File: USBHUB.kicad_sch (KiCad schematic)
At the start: 0 parts

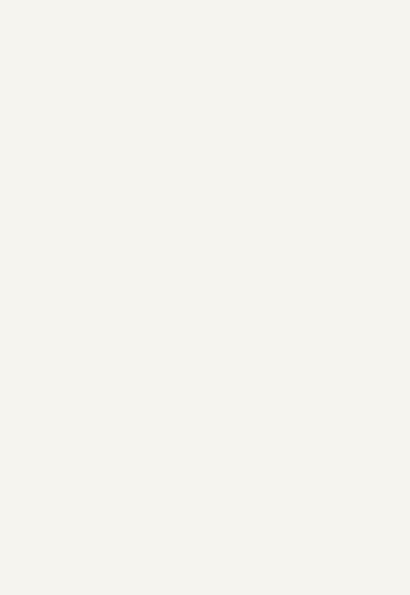
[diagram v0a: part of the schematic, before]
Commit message: finish PD controller schematic
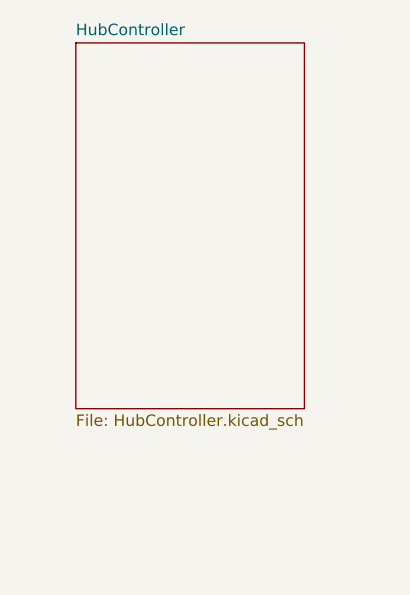
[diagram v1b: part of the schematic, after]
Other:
- added sheet HubController (HubController.kicad_sch)
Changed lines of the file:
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@@
     (title "USB Hub")
+  )
+  (sheet (at 31.75 50.8) (size 25.4 40.64) (fields_autoplaced)
+    (stroke (width 0.1524) (type solid))
+    (fill (color 0 0 0 0.0000))
+    (property "Sheetname" "HubController" (at 31.75 50.0884 0)
+      (effects (font (size 1.27 1.27)) (justify left bottom))
+    )
+    (property "Sheetfile" "HubController.kicad_sch" (at 31.75 92.0246 0)
+      (effects (font (size 1.27 1.27)) (justify left top))
+    )
+    (instances
+      (project "USBHUB"
+        (path "/d5edc647-9ac3-4ac1-ab8a-57c77be3f4d3" (page "3"))
+      )
+    )
   )
   (sheet (at 25.4 119.38) (size 21.59 35.56) (fields_autoplaced)

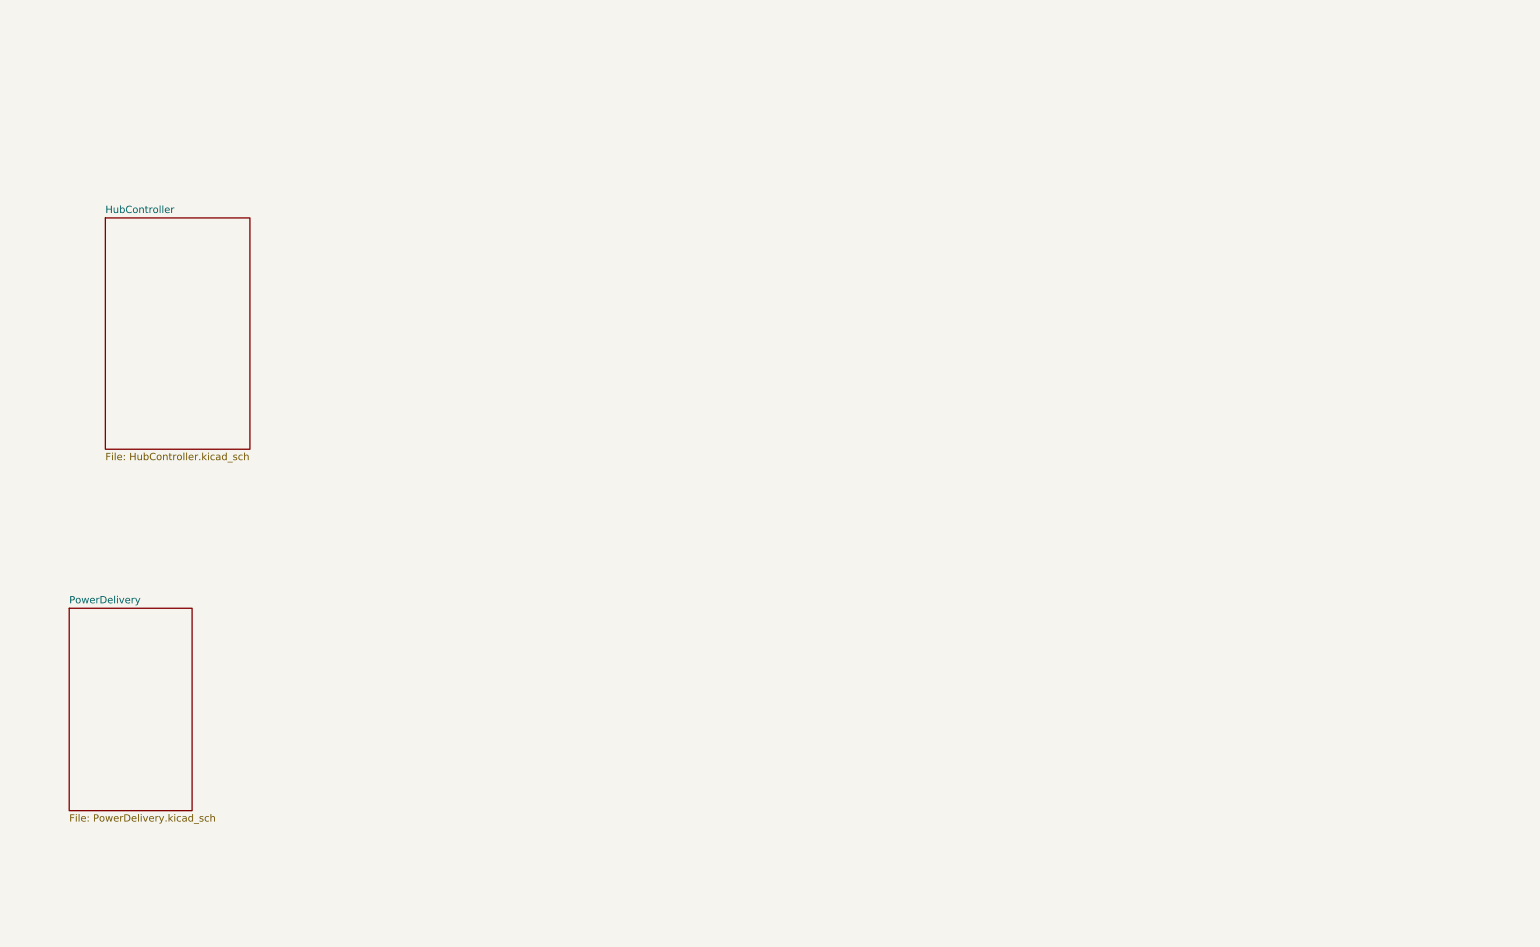
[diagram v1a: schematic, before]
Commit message: start layout of usb PD
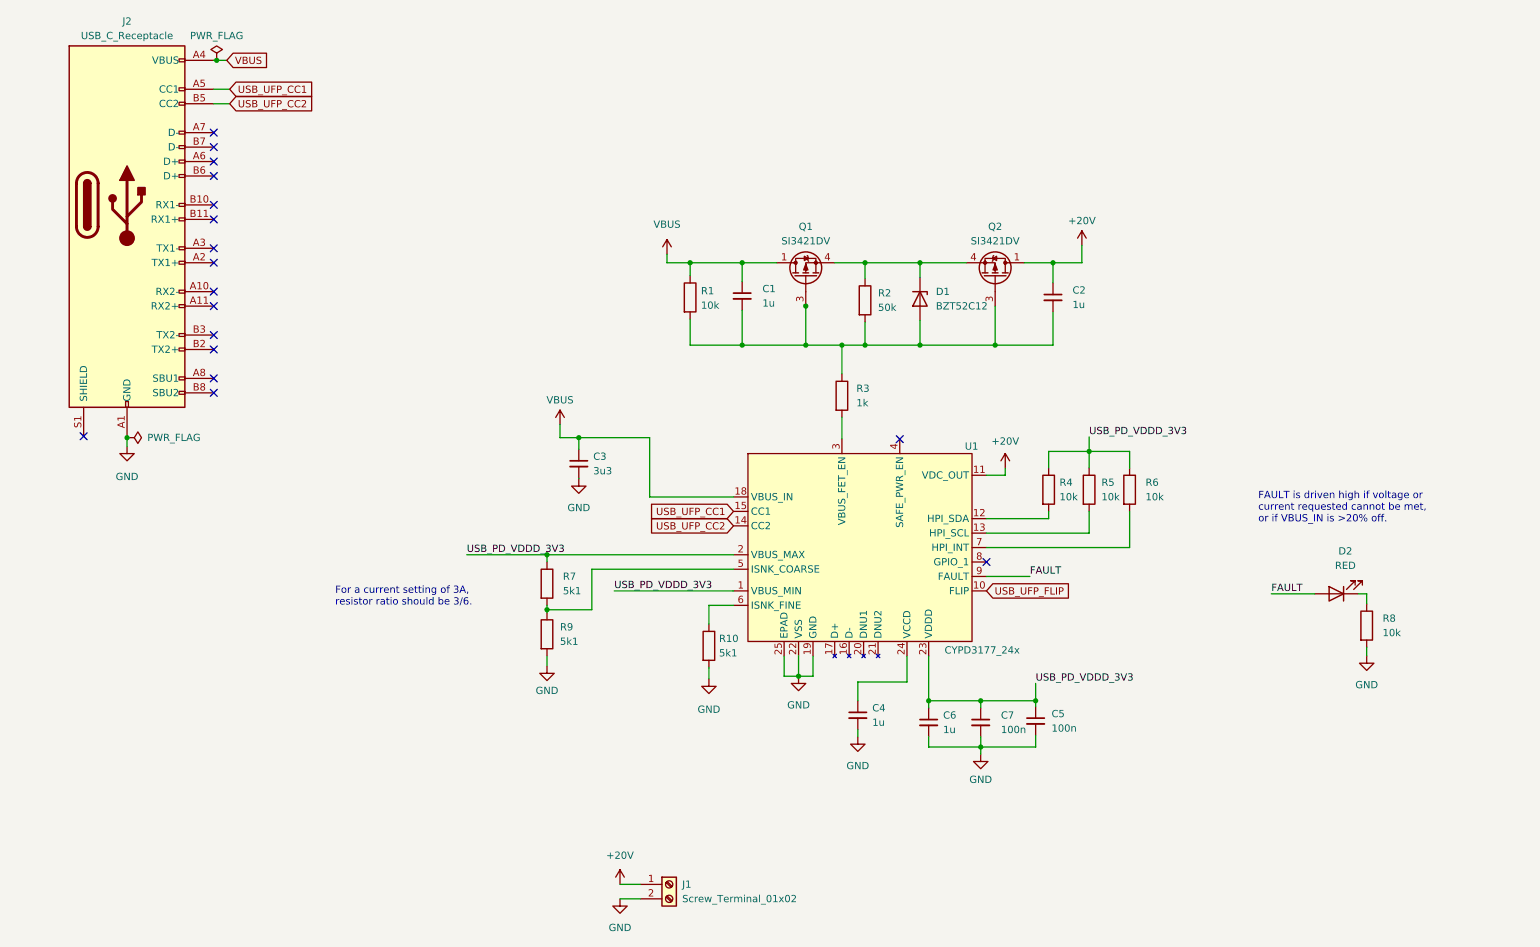
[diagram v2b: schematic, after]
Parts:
- added C1, C2, C4, C6: 1u, Capacitor_SMD:C_0603_1608Metric, symbol Device:C_Small
- added C3: 3u3, Capacitor_SMD:C_0603_1608Metric, symbol Device:C_Small
- added C5, C7: 100n, Capacitor_SMD:C_0603_1608Metric, symbol Device:C_Small
- added D1: BZT52C12, Diode_SMD:D_SOD-123, symbol Device:D_Zener
- added D2: RED, LED_SMD:LED_0603_1608Metric, symbol Device:LED
- added J1: Screw_Terminal_01x02, TerminalBlock_Phoenix:TerminalBlock_Phoenix_MKDS-1,5-2-5.08_1x02_P5.08mm_Horizontal, symbol Connector:Screw_Terminal_01x02
- added J2: USB_C_Receptacle, Cake_USB:USB_C_Receptacle_GT-USB-7052, symbol Connector:USB_C_Receptacle
- added Q1, Q2: SI3421DV, Package_TO_SOT_SMD:SOT-23-6, symbol catSink:SI3421DV
- added R1, R4, R5, R6, R8: 10k, Resistor_SMD:R_0603_1608Metric, symbol Device:R
- added R10, R7, R9: 5k1, Resistor_SMD:R_0603_1608Metric, symbol Device:R
- added R2: 50k, Resistor_SMD:R_0603_1608Metric, symbol Device:R
- added R3: 1k, Resistor_SMD:R_0603_1608Metric, symbol Device:R
- added U1: CYPD3177_24x, Cake_USB:CYPD3177_24LQx_QFN-24_EP_4x4_Pitch0.5mm, symbol Cake_USB:CYPD3177_24x
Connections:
- new net: D1.1 (K), Q1.4 (S), Q2.4 (S), R2.1
- new net: C1.2, C2.2, D1.2 (A), Q1.3 (G), Q2.3 (G), R1.2, R2.2, R3.1
- new net: R5.2, U1.13 (HPI_SCL)
- new net: R7.2, R9.1, U1.5 (ISNK_COARSE)
- new net: R4.2, U1.12 (HPI_SDA)
- new net: D2.1 (K), R8.1
- new net: C4.1, U1.24 (VCCD)
- new net: R3.2, U1.3 (VBUS_FET_EN)
- new net: R10.1, U1.6 (ISNK_FINE)
- new net: R6.2, U1.7 (HPI_INT)
- new net +20V: C2.1, J1.1 (Pin_1), Q2.1 (D), Q2.2 (D1), Q2.5 (D2), Q2.6 (D3), U1.11 (VDC_OUT)
- new net FAULT: D2.2 (A), U1.9 (FAULT)
- new net GND: C3.2, C4.2, C5.2, C6.2, C7.2, J1.2 (Pin_2), J2.A1 (GND), J2.A12 (GND), J2.B1 (GND), J2.B12 (GND), R10.2, R8.2, R9.2, U1.19 (GND), U1.22 (VSS), U1.25 (EPAD)
- new net USB_PD_VDDD_3V3: C5.1, C6.1, C7.1, R4.1, R5.1, R6.1, R7.1, U1.1 (VBUS_MIN), U1.2 (VBUS_MAX), U1.23 (VDDD)
- new net USB_UFP_CC1: J2.A5 (CC1), U1.15 (CC1)
- new net USB_UFP_CC2: J2.B5 (CC2), U1.14 (CC2)
- new net USB_UFP_FLIP: U1.10 (FLIP)
- new net VBUS: C1.1, C3.1, J2.A4 (VBUS), J2.A9 (VBUS), J2.B4 (VBUS), J2.B9 (VBUS), Q1.1 (D), Q1.2 (D1), Q1.5 (D2), Q1.6 (D3), R1.1, U1.18 (VBUS_IN)
- no-connect marks 0 -> 17
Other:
- removed sheet HubController
- removed sheet PowerDelivery
- note added: "FAULT is driven high if voltage or current requested cannot be met, or if VBUS_IN is >20% off."
- note added: "For a current setting of 3A, resistor ratio should be 3/6."
- title: USB Hub -> USB PD

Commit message: Finish PCB design
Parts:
- added C8: 3u3, Capacitor_SMD:C_0603_1608Metric, symbol Device:C_Small
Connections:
- net +20V: now also J1.2 (Pin_2), C8.1; no longer J1.1 (Pin_1)
- net GND: now also J1.1 (Pin_1), C8.2; no longer J1.2 (Pin_2)
- net USB_UFP_FLIP: no longer names the net of U1.10 (FLIP)
- no-connect marks 17 -> 18
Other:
- moved on the sheet: D2, J1, R8

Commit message: some touchups
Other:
- note added: "FAULT LED"
- note added: "USB P/D 20V/3A"
- moved on the sheet: C8, J1, J2

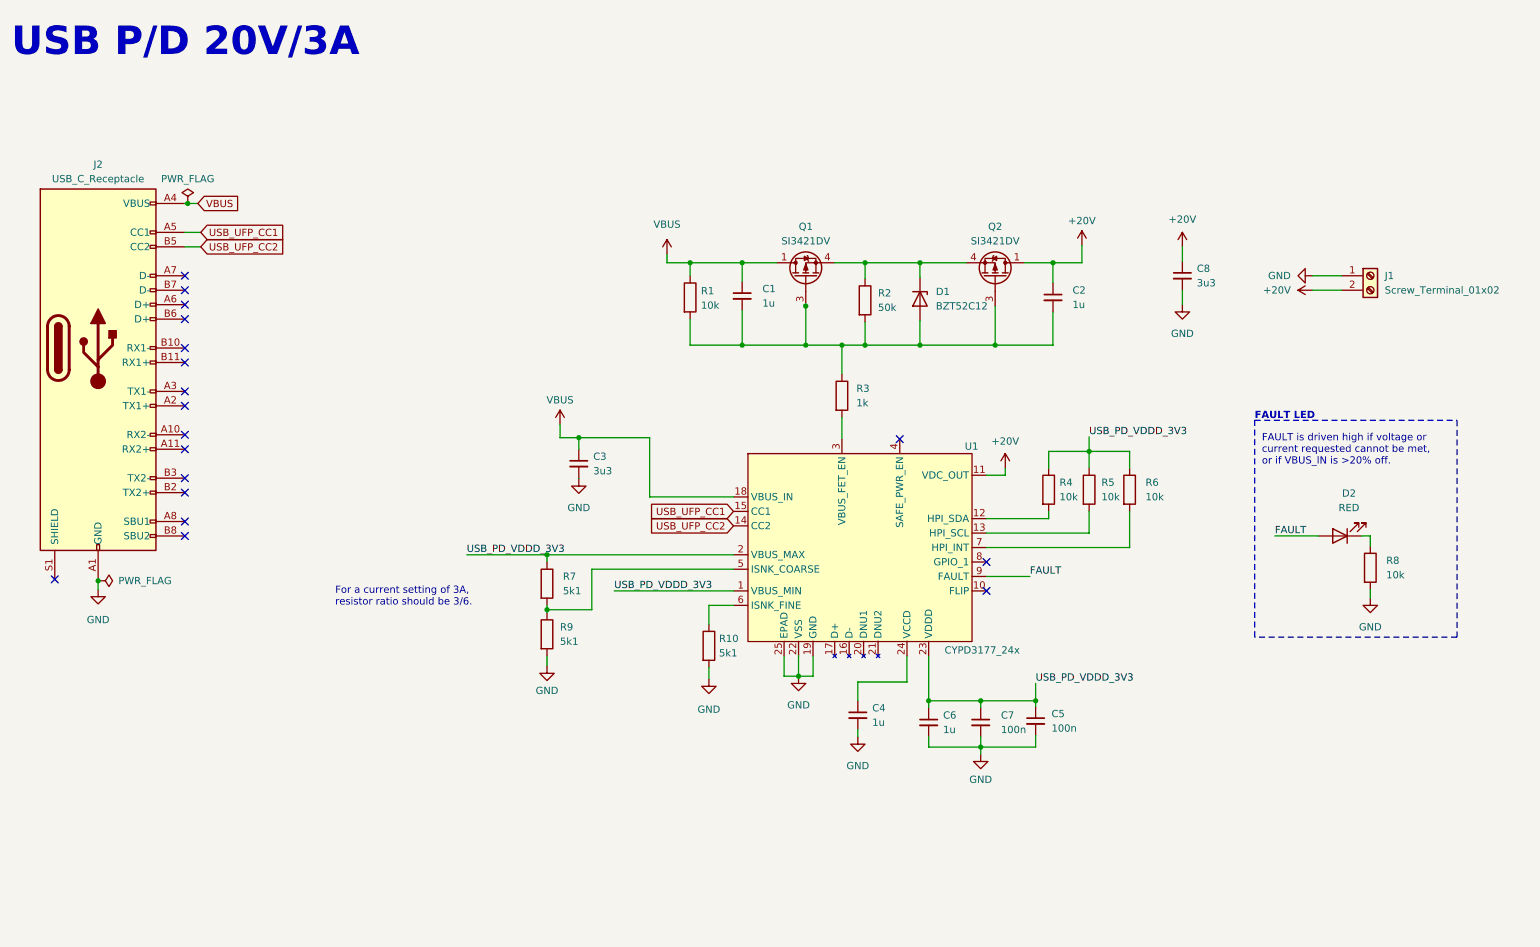
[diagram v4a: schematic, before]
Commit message: Add ESD for usb parts research, add TUSB522P and PI3USB302
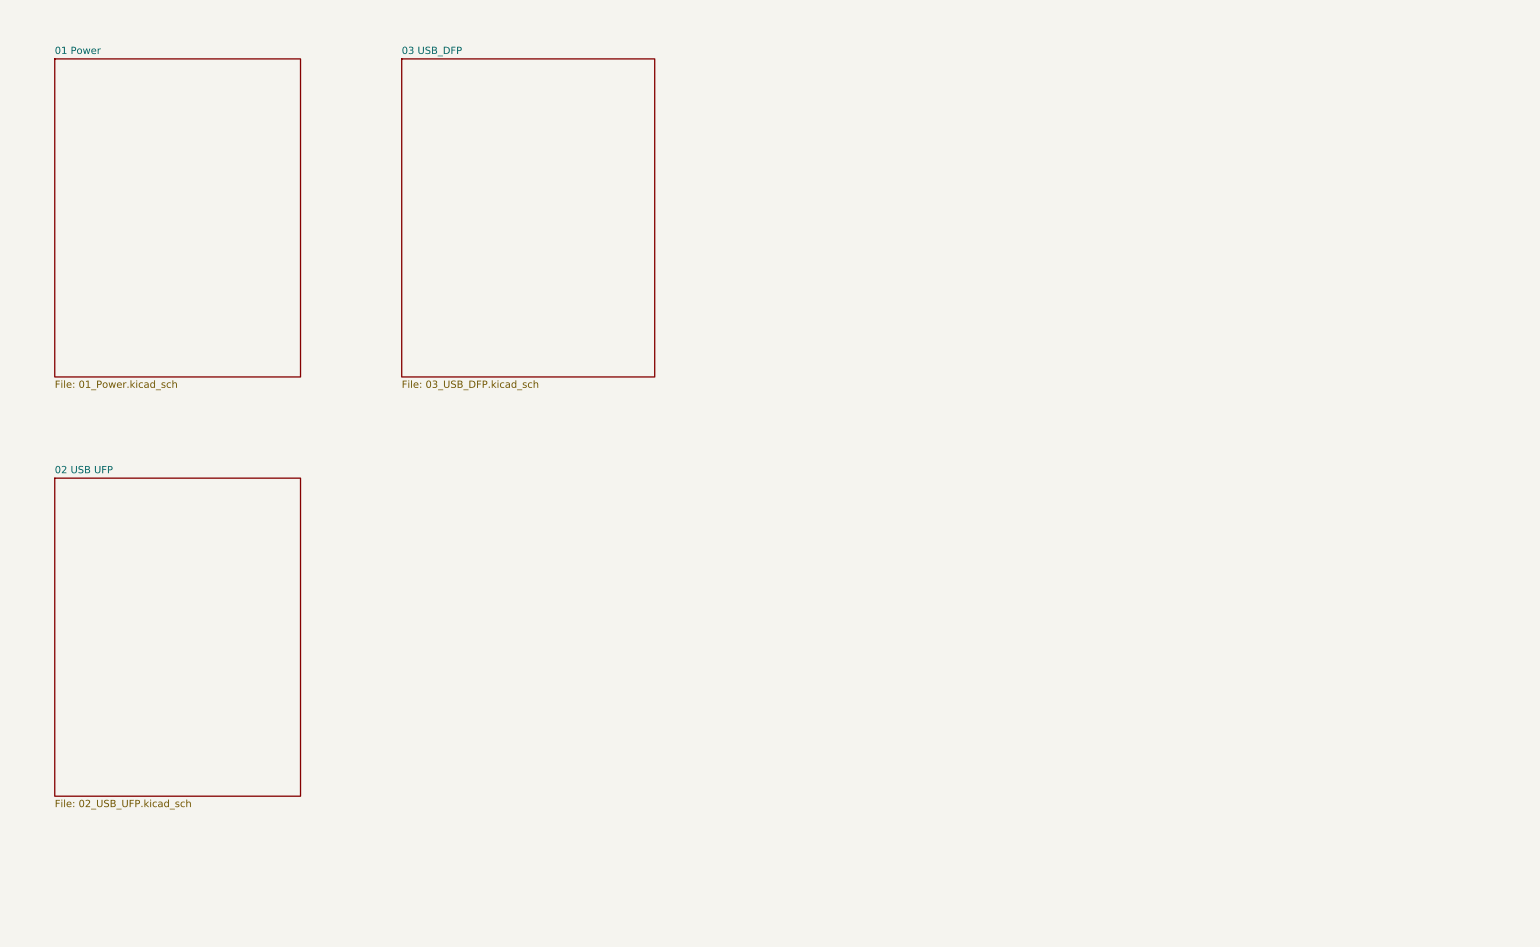
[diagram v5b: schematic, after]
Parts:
- removed C1, C2, C4, C6: 1u, Capacitor_SMD:C_0603_1608Metric, symbol Device:C_Small
- removed C3, C8: 3u3, Capacitor_SMD:C_0603_1608Metric, symbol Device:C_Small
- removed C5, C7: 100n, Capacitor_SMD:C_0603_1608Metric, symbol Device:C_Small
- removed D1: BZT52C12, Diode_SMD:D_SOD-123, symbol Device:D_Zener
- removed D2: RED, LED_SMD:LED_0603_1608Metric, symbol Device:LED
- removed J1: Screw_Terminal_01x02, TerminalBlock_Phoenix:TerminalBlock_Phoenix_MKDS-1,5-2-5.08_1x02_P5.08mm_Horizontal, symbol Connector:Screw_Terminal_01x02
- removed J2: USB_C_Receptacle, Cake_USB:USB_C_Receptacle_GT-USB-7052, symbol Connector:USB_C_Receptacle
- removed Q1, Q2: SI3421DV, Package_TO_SOT_SMD:SOT-23-6, symbol catSink:SI3421DV
- removed R1, R4, R5, R6, R8: 10k, Resistor_SMD:R_0603_1608Metric, symbol Device:R
- removed R10, R7, R9: 5k1, Resistor_SMD:R_0603_1608Metric, symbol Device:R
- removed R2: 50k, Resistor_SMD:R_0603_1608Metric, symbol Device:R
- removed R3: 1k, Resistor_SMD:R_0603_1608Metric, symbol Device:R
- removed U1: CYPD3177_24x, Cake_USB:CYPD3177_24LQx_QFN-24_EP_4x4_Pitch0.5mm, symbol Cake_USB:CYPD3177_24x
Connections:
- no-connect marks 18 -> 0
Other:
- added sheet 01 Power (01_Power.kicad_sch)
- added sheet 02 USB UFP (02_USB_UFP.kicad_sch)
- added sheet 03 USB_DFP (03_USB_DFP.kicad_sch)
- note removed: "FAULT LED"
- note removed: "FAULT is driven high if voltage or current requested cannot be met, or if VBUS_IN is >20% off."
- note removed: "For a current setting of 3A, resistor ratio should be 3/6."
- note removed: "USB P/D 20V/3A"
- title: USB PD -> USB 3.0 Hub 

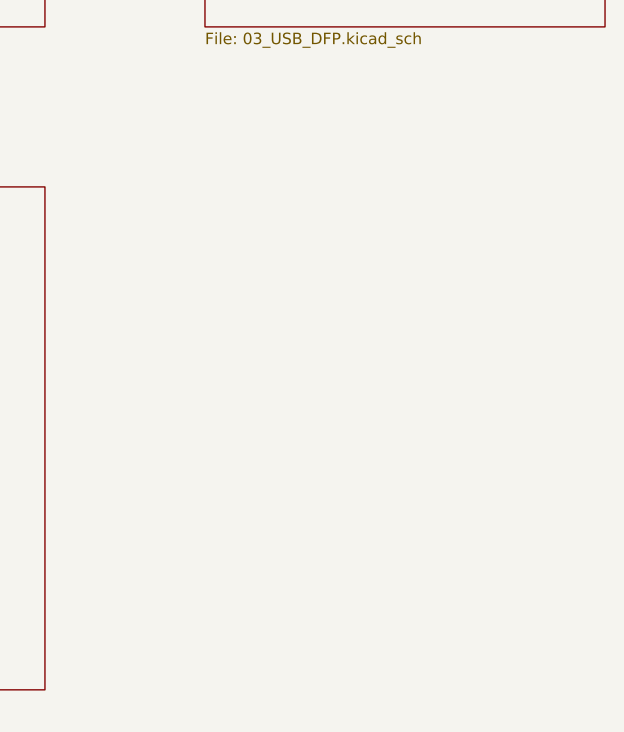
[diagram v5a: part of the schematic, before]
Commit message: Add ESD protection for UFP, create buck converter model
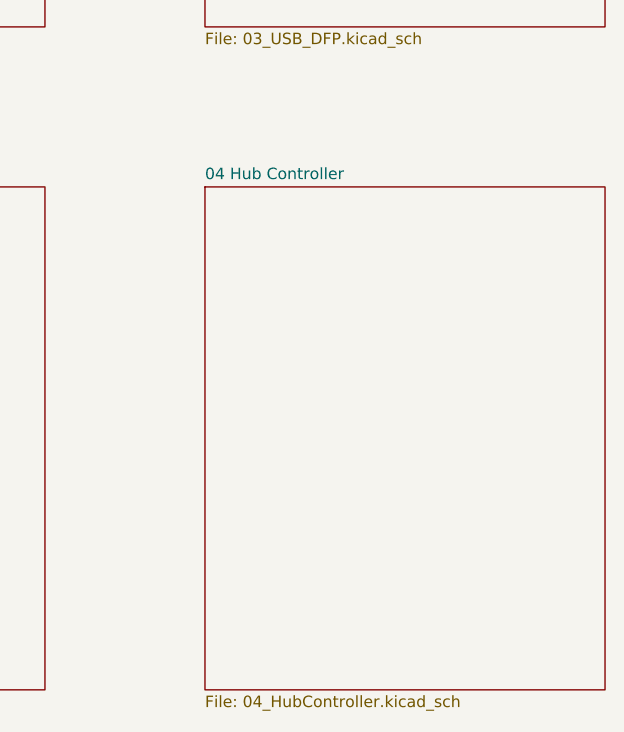
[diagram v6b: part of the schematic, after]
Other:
- added sheet 04 Hub Controller (04_HubController.kicad_sch)
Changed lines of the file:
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@@
+    )
+  )
+  (sheet (at 83.82 96.52) (size 44.45 55.88) (fields_autoplaced)
+    (stroke (width 0.1524) (type solid))
+    (fill (color 0 0 0 0.0000))
+    (property "Sheetname" "04 Hub Controller" (at 83.82 95.8084 0)
+      (effects (font (size 1.27 1.27)) (justify left bottom))
+    )
+    (property "Sheetfile" "04_HubController.kicad_sch" (at 83.82 152.9846 0)
+      (effects (font (size 1.27 1.27)) (justify left top))
+    )
+    (instances
+      (project "USBHUB"
+        (path "/d5edc647-9ac3-4ac1-ab8a-57c77be3f4d3" (page "6"))
+      )
     )
   )
